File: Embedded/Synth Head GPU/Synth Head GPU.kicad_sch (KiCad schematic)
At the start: 25 parts, among them J1 10171746-00021LF, U11 SRV05-4

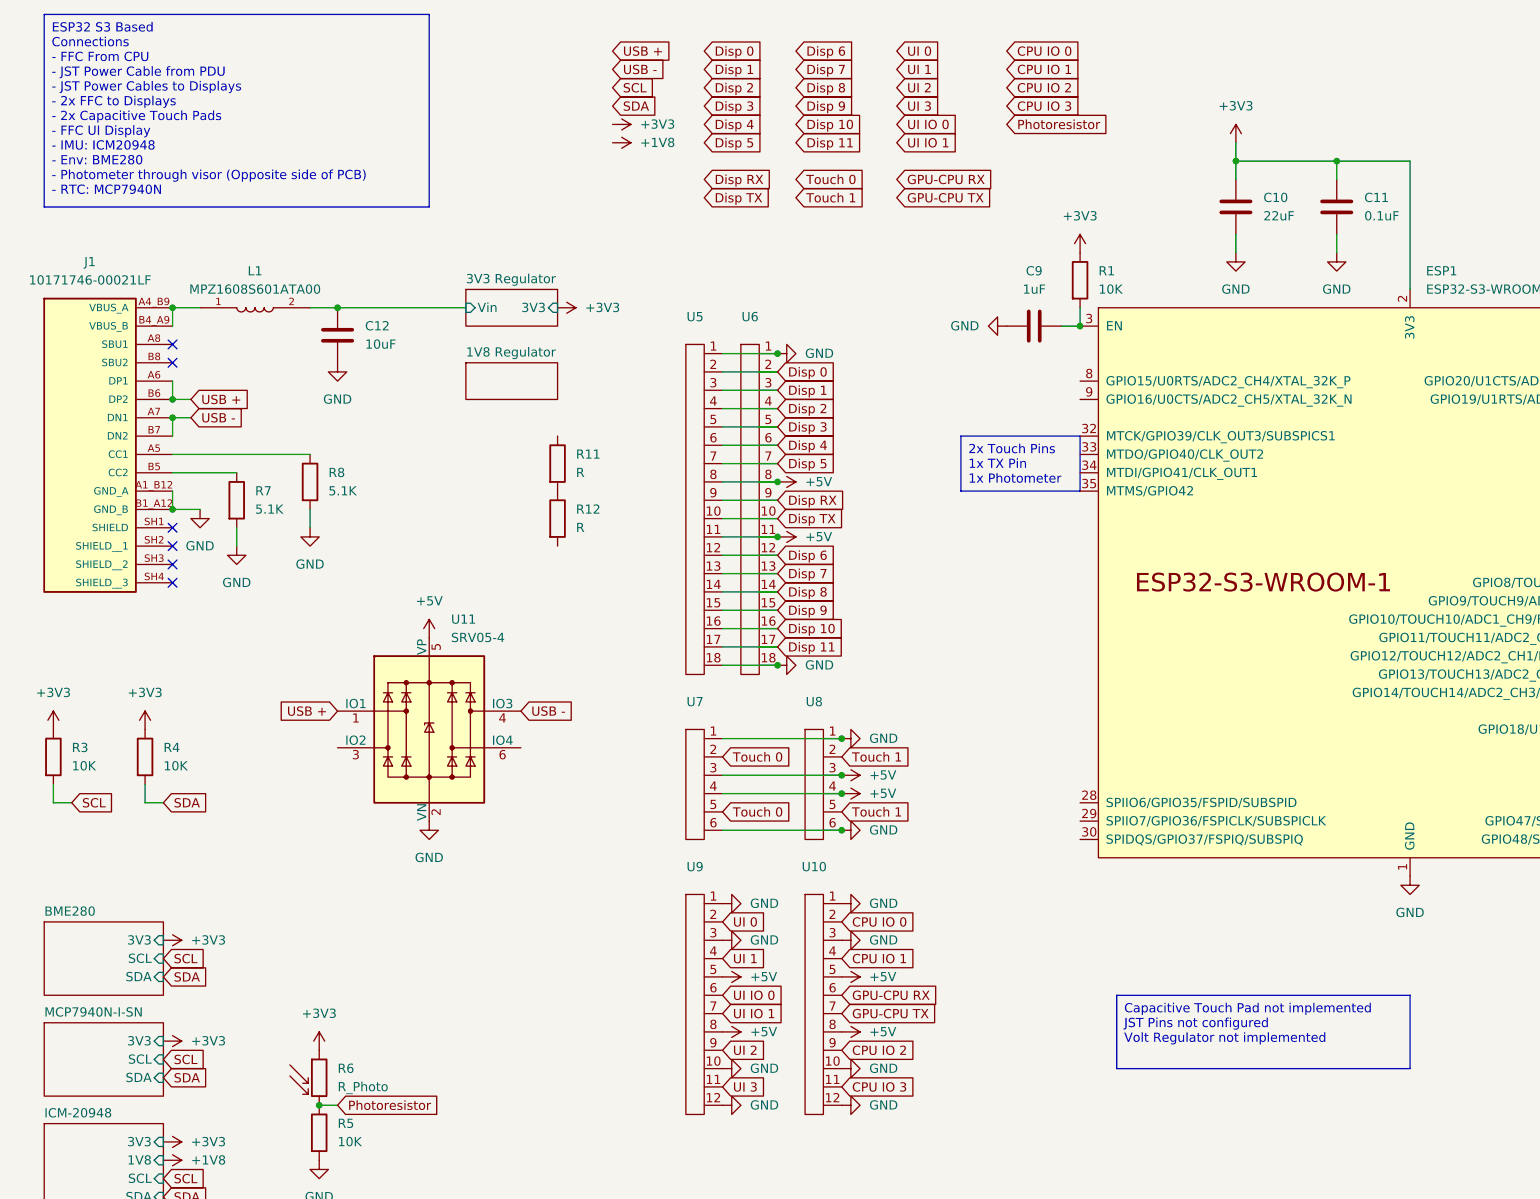
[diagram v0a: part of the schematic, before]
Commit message: GPU Port Assignments & Sensors Confirmed
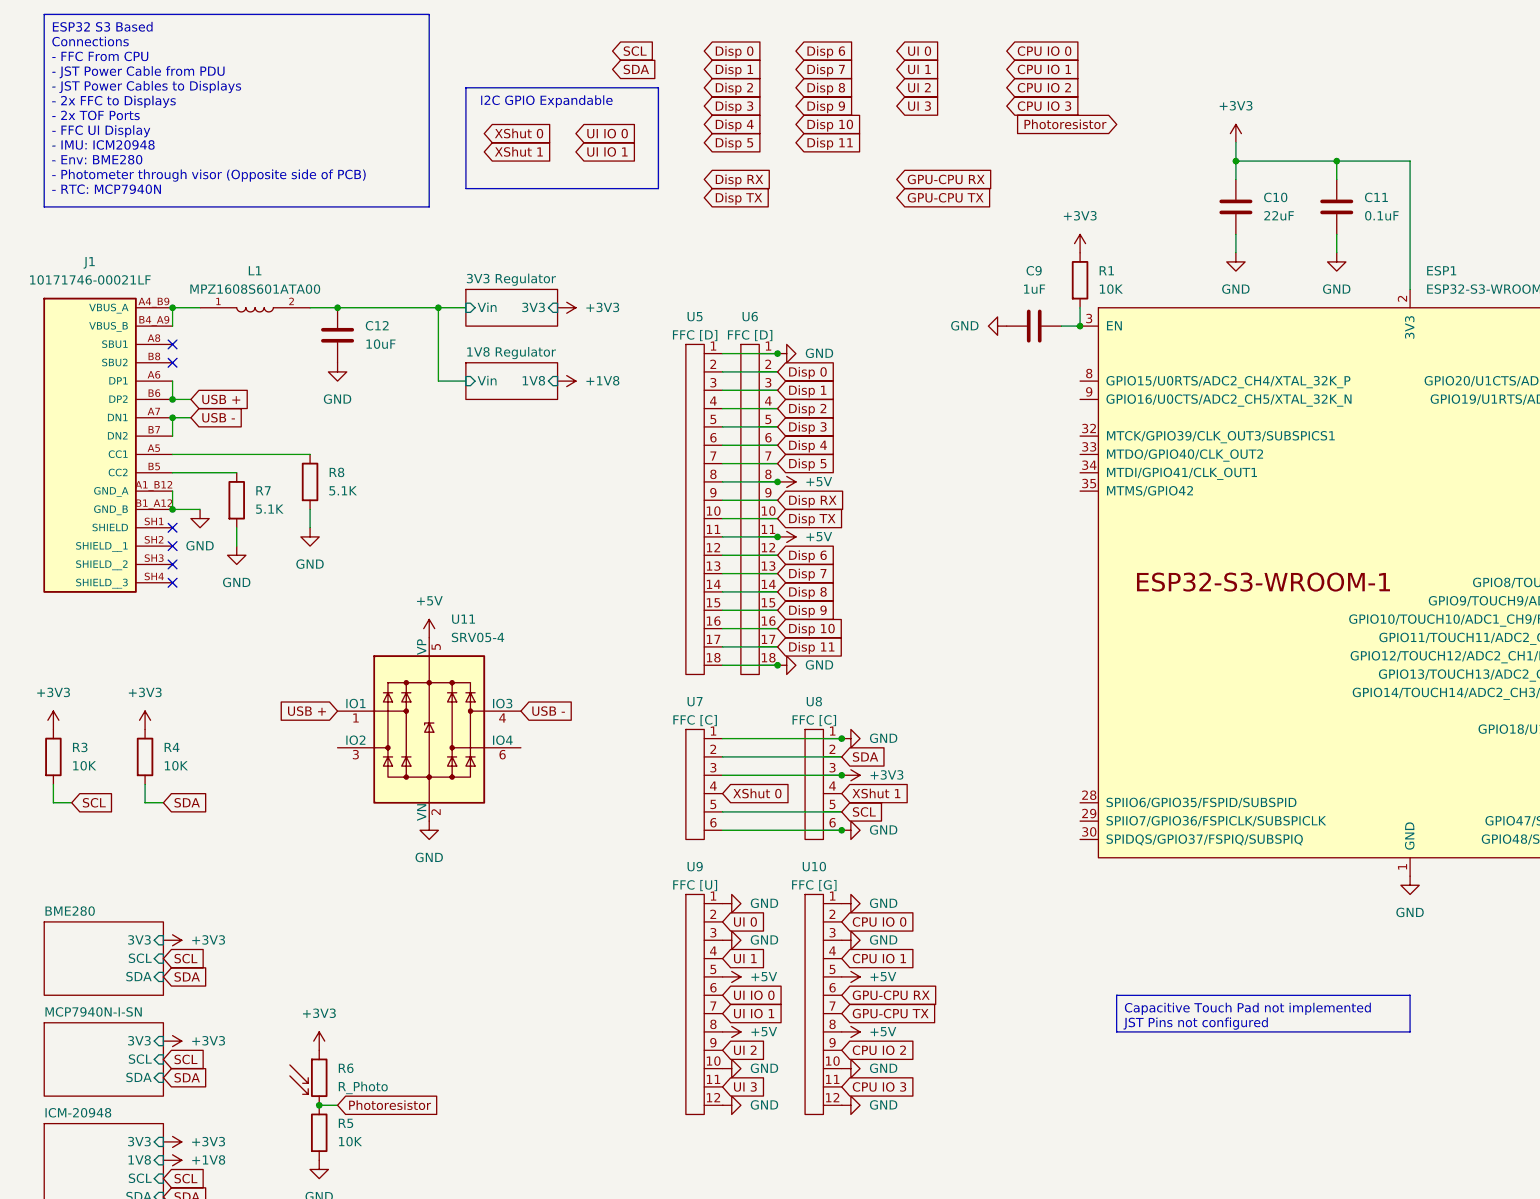
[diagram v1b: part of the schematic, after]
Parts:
- removed R11, R12: R, symbol Device:R
- U10: value ~ -> FFC [G]
- U5, U6: value ~ -> FFC [D]
- U7, U8: value ~ -> FFC [C]
- U9: value ~ -> FFC [U]; footprint (none) -> FFC_Connector:FFC Aliexpress 0.5mm 12P
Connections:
- net +3V3: now also U7.3, U8.3
- net +5V: no longer U7.3, U7.4, U8.3, U8.4
- net SCL: now also U7.5, U8.5
- net SDA: now also U7.2, U8.2
- net 3V3 Regulator/Vin renamed 1V8 Regulator/Vin
- removed net Touch 0: U7.2, U7.5
- removed net Touch 1: U8.2, U8.5
- new net XShut 0: U7.4
- new net XShut 1: U8.4
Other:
- sheet 1V8 Regulator ports: added 1V8, Vin; removed none
- note added: "I2C GPIO Expandable"

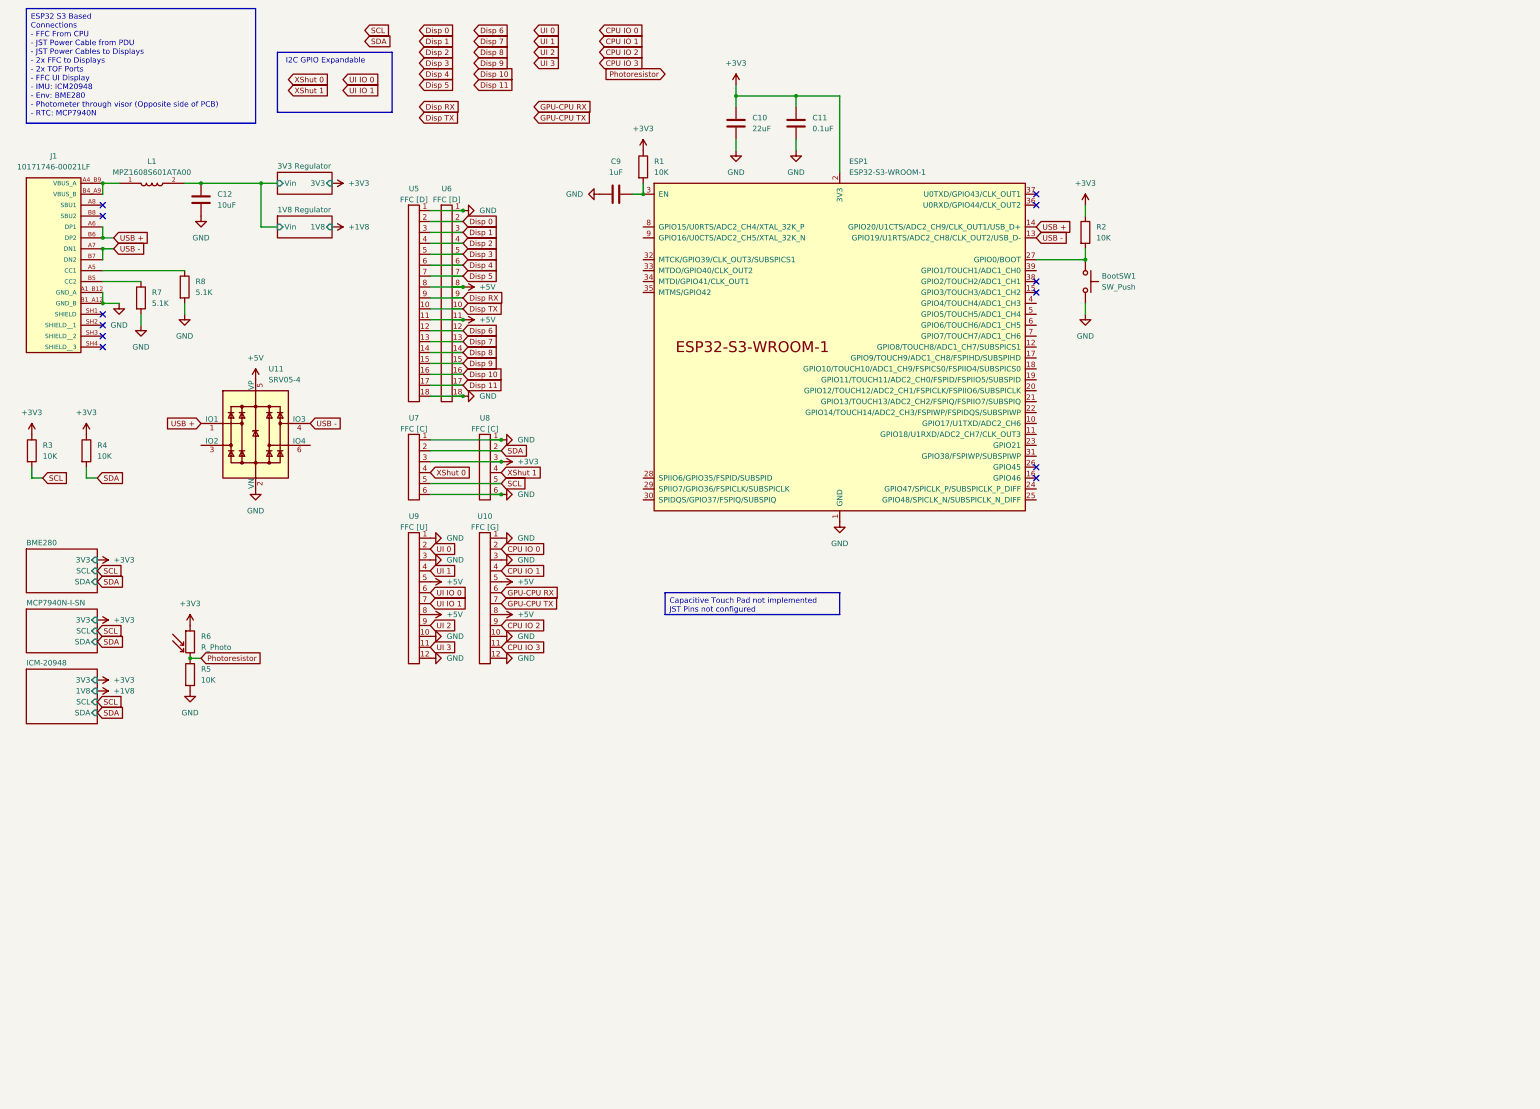
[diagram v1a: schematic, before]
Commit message: Added I2C GPIO Expansion to GPU & Some Pin Position Updates
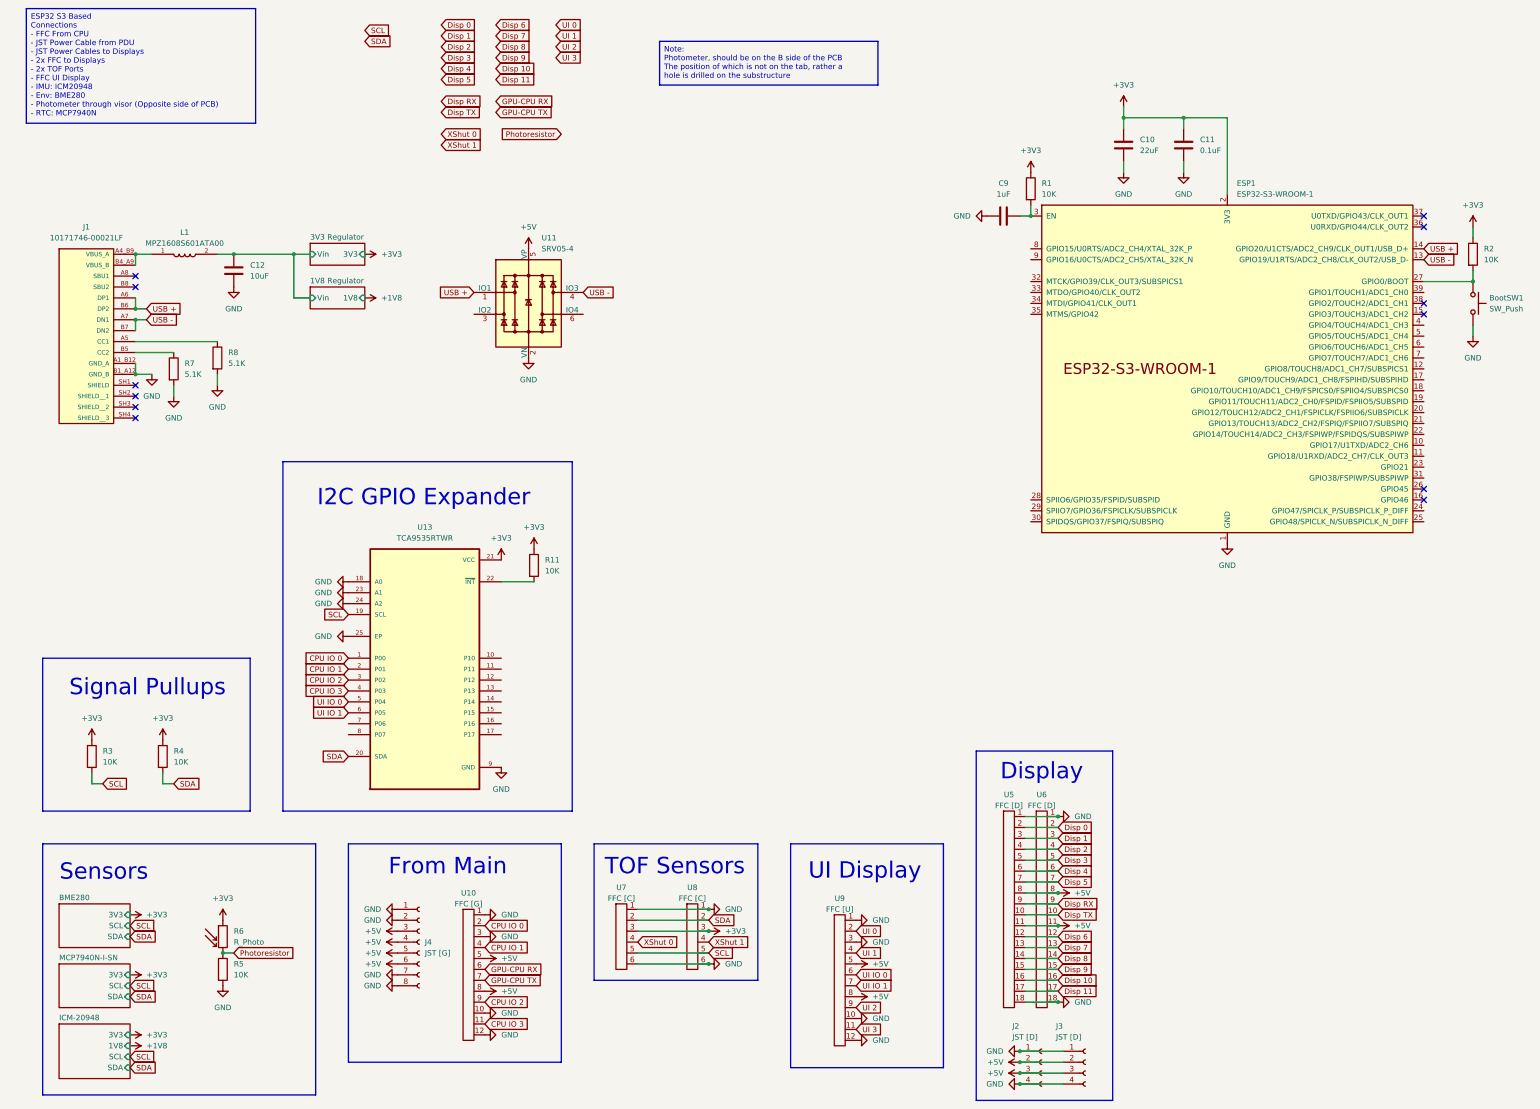
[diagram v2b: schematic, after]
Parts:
- added J2, J3: JST [D], symbol Connector:Conn_01x04_Socket
- added J4: JST [G], symbol Connector:Conn_01x08_Socket
- added R11: 10K, Resistor_SMD:R_0603_1608Metric, symbol Device:R
- added U13: TCA9535RTWR, TCA9535RTWR:QFN50P400X400X80-25N, symbol IO_Expander_TCA9535RTWR:TCA9535RTWR
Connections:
- net +3V3: now also R11.1, U13.21 (VCC)
- net +5V: now also J2.2 (Pin_2), J2.3 (Pin_3), J3.2 (Pin_2), J3.3 (Pin_3), J4.3 (Pin_3), J4.4 (Pin_4), J4.5 (Pin_5), J4.6 (Pin_6)
- net CPU IO 0: now also U13.1 (P00)
- net CPU IO 1: now also U13.2 (P01)
- net CPU IO 2: now also U13.3 (P02)
- net CPU IO 3: now also U13.4 (P03)
- net GND: now also J2.1 (Pin_1), J2.4 (Pin_4), J3.1 (Pin_1), J3.4 (Pin_4), J4.1 (Pin_1), J4.2 (Pin_2), J4.7 (Pin_7), J4.8 (Pin_8), U13.18 (A0), U13.23 (A1), U13.24 (A2), U13.25 (EP), U13.9 (GND)
- net SCL: now also U13.19 (SCL)
- net SDA: now also U13.20 (SDA)
- net UI IO 0: now also U13.5 (P04)
- net UI IO 1: now also U13.6 (P05)
- new net: R11.2, U13.22 (~{INT})
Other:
- note added: "Display"
- note added: "From Main"
- note added: "I2C GPIO Expander"
- note added: "Sensors"
- note added: "Signal Pullups"
- note added: "TOF Sensors"
- note added: "UI Display"
- note removed: "I2C GPIO Expandable"
- moved on the sheet: BootSW1, C10, C11, C12, C9, ESP1, J1, L1, R1, R2, R3, R4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
